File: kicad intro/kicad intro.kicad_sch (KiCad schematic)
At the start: 13 parts, among them J1 USB_C_Receptacle_PowerOnly_6P, J2 Conn_01x03_Socket, J3 Conn_01x03_Socket, Q1 BF459, U1 ATtiny85-20P

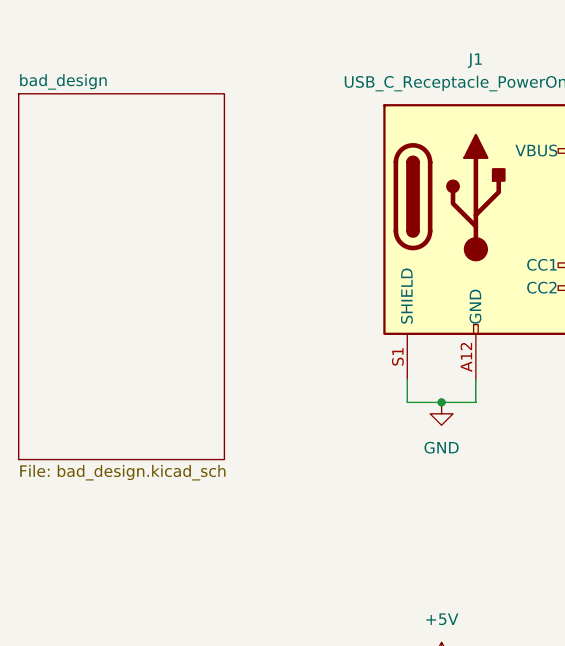
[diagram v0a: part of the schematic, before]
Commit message: Separated ground pours
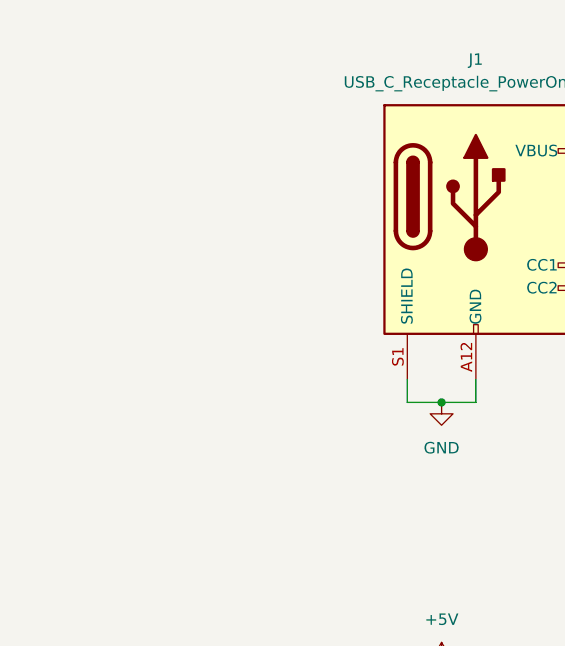
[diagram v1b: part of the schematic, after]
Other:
- removed sheet bad_design
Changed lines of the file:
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@@
-		)
-	)
-	(sheet
-		(at 22.86 52.07)
-		(size 22.86 40.64)
-		(exclude_from_sim no)
-		(in_bom yes)
-		(on_board yes)
-		(dnp no)
-		(fields_autoplaced yes)
-		(stroke
-			(width 0.1524)
-			(type solid)
-		)
-		(fill
-			(color 0 0 0 0.0000)
-		)
-		(property "Sheetname" "bad_design"
-			(at 22.86 51.3584 0)
-			(effects
-				(font
-					(size 1.27 1.27)
-				)
-				(justify left bottom)
-			)
-		)
-		(property "Sheetfile" "bad_design.kicad_sch"
-			(at 22.86 93.2946 0)
-			(effects
-				(font
-					(size 1.27 1.27)
-				)
-				(justify left top)
-			)
-		)
-		(instances
-			(project "kicad intro"
-				(path "/32588871-82df-415f-b692-9d5306434797"
-					(page "2")
-				)
-			)
 		)
 	)

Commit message: Updated sample code and design
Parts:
- removed D2: LED, LED_THT:LED_D3.0mm, symbol Device:LED
- removed R1: 220, Resistor_THT:R_Axial_DIN0207_L6.3mm_D2.5mm_P7.62mm_Horizontal, symbol Device:R
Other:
- note removed: "Error LED"
